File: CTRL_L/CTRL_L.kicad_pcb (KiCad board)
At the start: 2 copper layers, 33.8 x 93.2 mm, 22 parts, among them J1 BM14B-NSHSS-TBT_LF__SN_, J2 BM04B-NSHSS-TBT_LF__SN_, J3 BM04B-NSHSS-TBT_LF__SN_, SW3 SW_Push, SW4 SW_Push, SW5 SW_Push, SW6 SW_Push, SW7 SW_Push

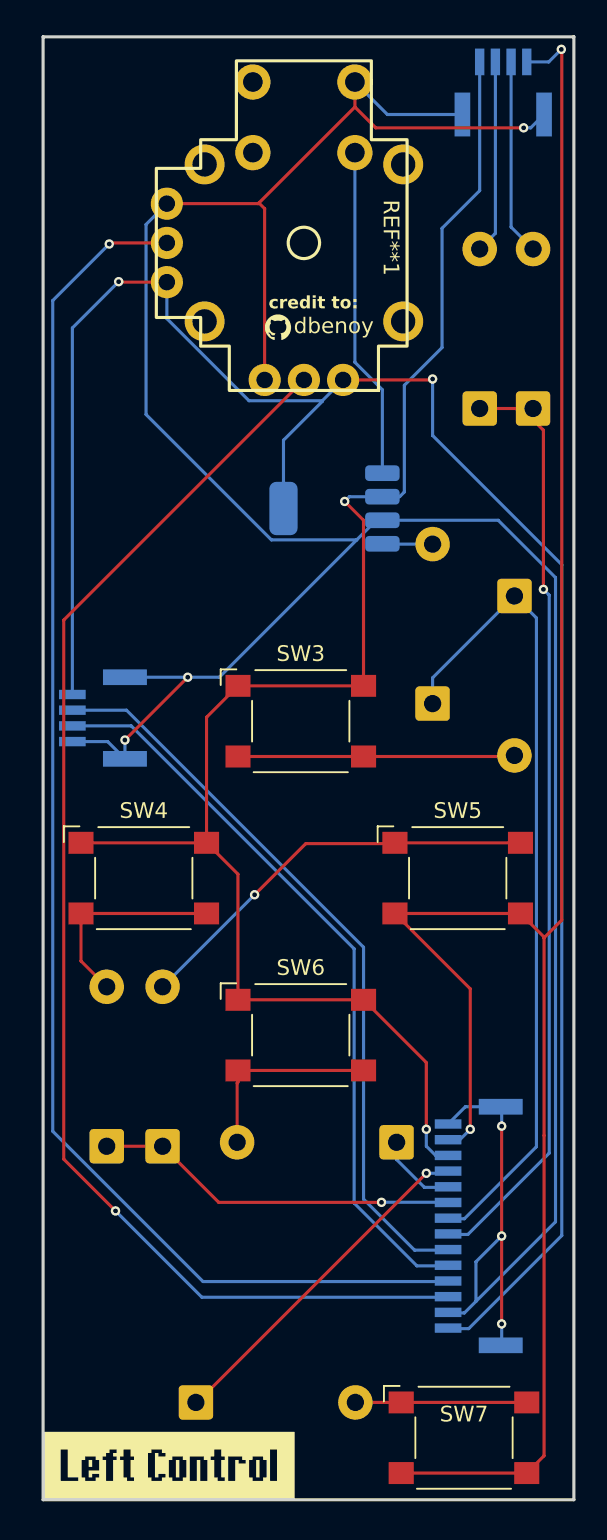
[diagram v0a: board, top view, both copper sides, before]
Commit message: CTRL_L updated to use new Diodes.
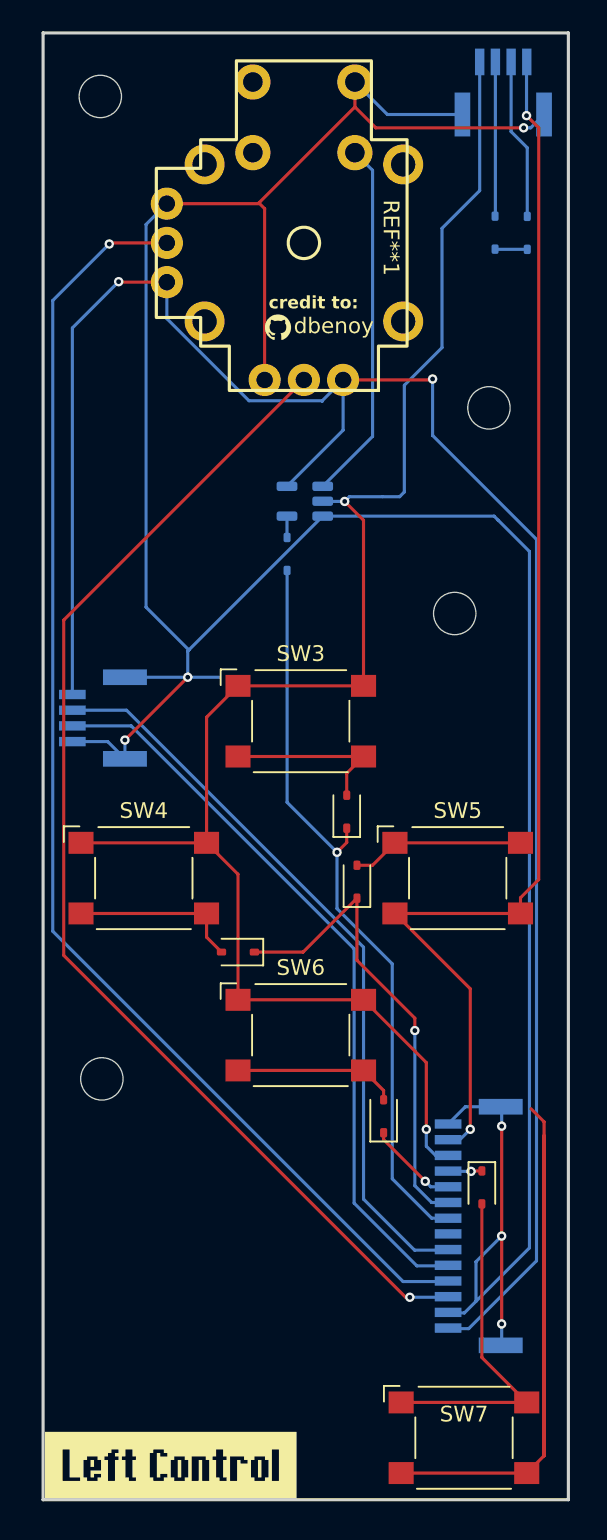
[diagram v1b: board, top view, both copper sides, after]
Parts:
- removed AND1: 74AHC1G08, Package_TO_SOT_SMD:SOT-223-5
- added REF**: M2.5_2.7mm, MountingHole:MountingHole_2.7mm_M2.5, F.Cu at (158.2, 72.1)
- added REF**: M2.5_2.7mm, MountingHole:MountingHole_2.7mm_M2.5, F.Cu at (135.6, 39.2)
- added REF**: M2.5_2.7mm, MountingHole:MountingHole_2.7mm_M2.5, F.Cu at (135.7, 101.8)
- added REF**: M2.5_2.7mm, MountingHole:MountingHole_2.7mm_M2.5, F.Cu at (160.4, 59.0)
- added U1: 74LVC1G08, Package_TO_SOT_SMD:SOT-23-5, B.Cu at (148.7, 65.0)
- D1, D2, D8: value 1N4001 -> 1N4148WS; footprint Diode_THT:D_DO-41_SOD81_P10.16mm_Horizontal -> Diode_SMD:D_SOD-323
- D3, D4, D5, D6, D7: value 1N4001 -> 1N4148WS; footprint Diode_THT:D_DO-41_SOD81_P10.16mm_Horizontal -> Diode_SMD:D_SOD-323; moved to F.Cu
- moved D8 54.4 mm to (147.5, 68.3), turned to 90 degrees
- moved D4 28.7 mm to (144.4, 93.7), turned to 180 degrees
- moved D5 23.2 mm to (152.0, 89.2)
- moved D6 14.2 mm to (153.7, 104.2)
- moved D1 11.2 mm to (160.8, 47.9)
- moved D2 11.2 mm to (162.8, 47.9)
- moved D3 8.80 mm to (151.3, 84.8)
- moved D7 6.15 mm to (159.9, 108.7), turned to -90 degrees
- moved kibuzzard-6A187131 0.46 mm to (157.3, 126.4)
- moved kibuzzard-6A186FEC 0.12 mm to (140.1, 126.4)
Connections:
- D4 pad 1: Row2 -> Row3
- D6 pad 1: Row3 -> Row4
- D7 pad 1: Row4 -> Row5
- D8 pad 1: Row5 -> Row2
- SW3 pad 2: Net-(D4-A) -> Net-(D3-A)
- SW4 pad 2: Net-(D5-A) -> Net-(D4-A)
- SW5 pad 1: Net-(D6-A) -> Net-(D5-A)
- SW6 pad 2: Net-(D7-A) -> Net-(D6-A)
- SW7 pad 1: Net-(D8-A) -> Net-(D7-A)
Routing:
- net Row1: track 59.9 -> 2.06 mm, vias 1 -> 0
- net Row5: track 22.1 -> 2.17 mm
- net Net-(D6-A): track 26.6 -> 10.4 mm, vias 1 -> 0
- net Net-(D8-A): track 10.9 -> 1.36 mm
- net Net-(D7-A): track 12.8 -> 21.8 mm
- net /ADC_X: track 84.1 -> 76.5 mm
- net /ADC_Y: track 90.9 -> 83.4 mm
- net Row3: track 23.3 -> 30.4 mm
- net Net-(D3-A): track 4.01 -> 10.9 mm
- net Net-(D4-A): track 17.7 -> 10.9 mm
- net Row2: track 52.2 -> 48.0 mm, vias 0 -> 1
- net Col2: track 130.0 -> 132.6 mm
- net Net-(D1-A): track 12.3 -> 9.84 mm
- net Net-(D5-A): track 13.5 -> 11.0 mm
- net Net-(D2-A): track 12.5 -> 10.3 mm
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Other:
- board size 33.8 x 93.2 mm -> 33.5 x 93.4 mm

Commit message: Added New Images (\Images)
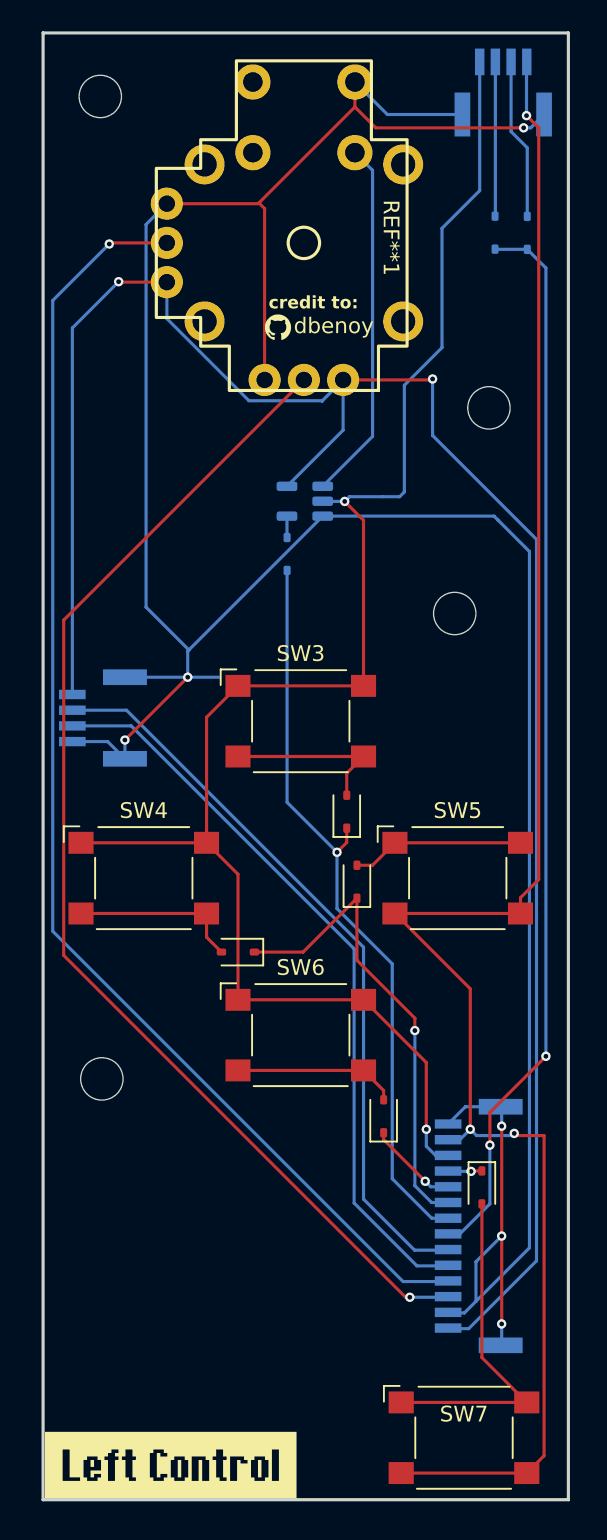
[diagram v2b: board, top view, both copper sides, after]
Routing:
- net Row1: track 2.06 -> 68.3 mm, vias 0 -> 2
- net Col2: track 132.6 -> 115.1 mm, vias 2 -> 3
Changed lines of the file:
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@@
-	)
-	(segment
-		(start 163.07 103.69)
-		(end 163.9 104.52)
-		(width 0.2)
-		(layer "F.Cu")
-		(net "Col2")
 	)
 	(segment
@@
 	)
 	(segment
+		(start 162.14 105.4)
+		(end 162 105.26)
+		(width 0.2)
+		(layer "F.Cu")
+		(net "Col2")
+	)
+	(segment
 		(start 162.4 91.25)
 		(end 162.4 91.64)
@@
 	)
 	(segment
+		(start 163.9 105.4)
+		(end 162.14 105.4)
+		(width 0.2)
+		(layer "F.Cu")
+		(net "Col2")
+	)
+	(segment
 		(start 162.783835 40.421406)
 		(end 163.56 41.197571)
@@
 		(net "Col2")
 	)
-	(segment
-		(start 163.9 104.52)
-		(end 163.9 125.8)
-		(width 0.2)
-		(layer "F.Cu")
-		(net "Col2")
-	)
 	(via
 		(at 159.2 105)
@@
 	)
 	(via
+		(at 162 105.26)
+		(size 0.6)
+		(drill 0.3)
+		(layers "F.Cu" "B.Cu")
+		(net "Col2")
+	)
+	(via
 		(at 162.783835 40.421406)
 		(size 0.6)
 		(drill 0.3)
 		(layers "F.Cu" "B.Cu")
+		(net "Col2")
+	)
+	(segment
+		(start 159.6 105.4)
+		(end 159.2 105)
+		(width 0.2)
+		(layer "B.Cu")
 		(net "Col2")
 	)
@@
 	)
 	(segment
+		(start 162 105.26)
+		(end 161.86 105.4)
+		(width 0.2)
+		(layer "B.Cu")
+		(net "Col2")
+	)
+	(segment
 		(start 162.783835 37.366163)
 		(end 162.8 37.349998)
@@
 	)
 	(segment
+		(start 161.86 105.4)
+		(end 159.6 105.4)
+		(width 0.2)
+		(layer "B.Cu")
+		(net "Col2")
+	)
+	(segment
+		(start 164.02 100.35)
+		(end 160.45 103.92)
+		(width 0.2)
+		(layer "F.Cu")
+		(net "Row1")
+	)
+	(segment
+		(start 160.45 103.92)
+		(end 160.45 106.01)
+		(width 0.2)
+		(layer "F.Cu")
+		(net "Row1")
+	)
+	(via
+		(at 164.02 100.35)
+		(size 0.6)
+		(drill 0.3)
+		(layers "F.Cu" "B.Cu")
+		(net "Row1")
+	)
+	(via
+		(at 160.45 106.01)
+		(size 0.6)
+		(drill 0.3)
+		(layers "F.Cu" "B.Cu")
+		(net "Row1")
+	)
+	(segment
+		(start 162.83 48.94)
+		(end 164.02 50.13)
+		(width 0.2)
+		(layer "B.Cu")
+		(net "Row1")
+	)
+	(segment
+		(start 164.02 50.13)
+		(end 164.02 100.35)
+		(width 0.2)
+		(layer "B.Cu")
+		(net "Row1")
+	)
+	(segment
+		(start 160.45 106.01)
+		(end 160.45 109.751823)
+		(width 0.2)
+		(layer "B.Cu")
+		(net "Row1")
+	)
+	(segment
+		(start 158.538901 111.662922)
+		(end 157.788901 111.662922)
+		(width 0.2)
+		(layer "B.Cu")
+		(net "Row1")
+	)
+	(segment
+		(start 160.45 109.751823)
+		(end 158.538901 111.662922)
+		(width 0.2)
+		(layer "B.Cu")
+		(net "Row1")
+	)
+	(segment

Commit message: Updated CTRL_L to use B3S-1000 Switches
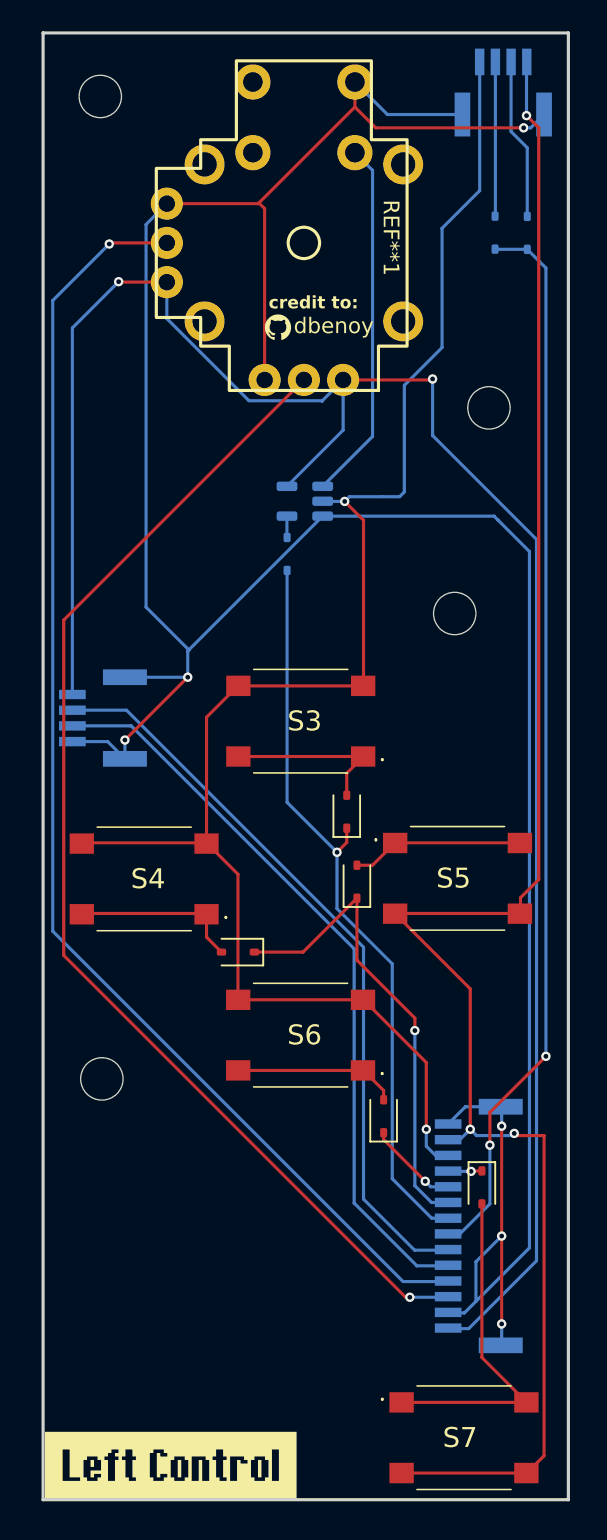
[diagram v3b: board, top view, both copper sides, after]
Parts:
- removed SW3, SW4, SW5, SW6, SW7: SW_Push, Button_Switch_SMD:SW_SPST_Omron_B3FS-100xP
- added S3: B3S-1000, B3S-1000:B3S1000, F.Cu at (148.4, 79.0)
- added S4: B3S-1000, B3S-1000:B3S1000, F.Cu at (138.4, 89.0)
- added S5: B3S-1000, B3S-1000:B3S1000, F.Cu at (158.4, 89.0)
- added S6: B3S-1000, B3S-1000:B3S1000, F.Cu at (148.4, 99.0)
- added S7: B3S-1000, B3S-1000:B3S1000, F.Cu at (158.8, 124.7)
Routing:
- net GND: track 197.9 -> 195.9 mm

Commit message: Mainboard Progress, Updated CTRL-L for new Joystick Module
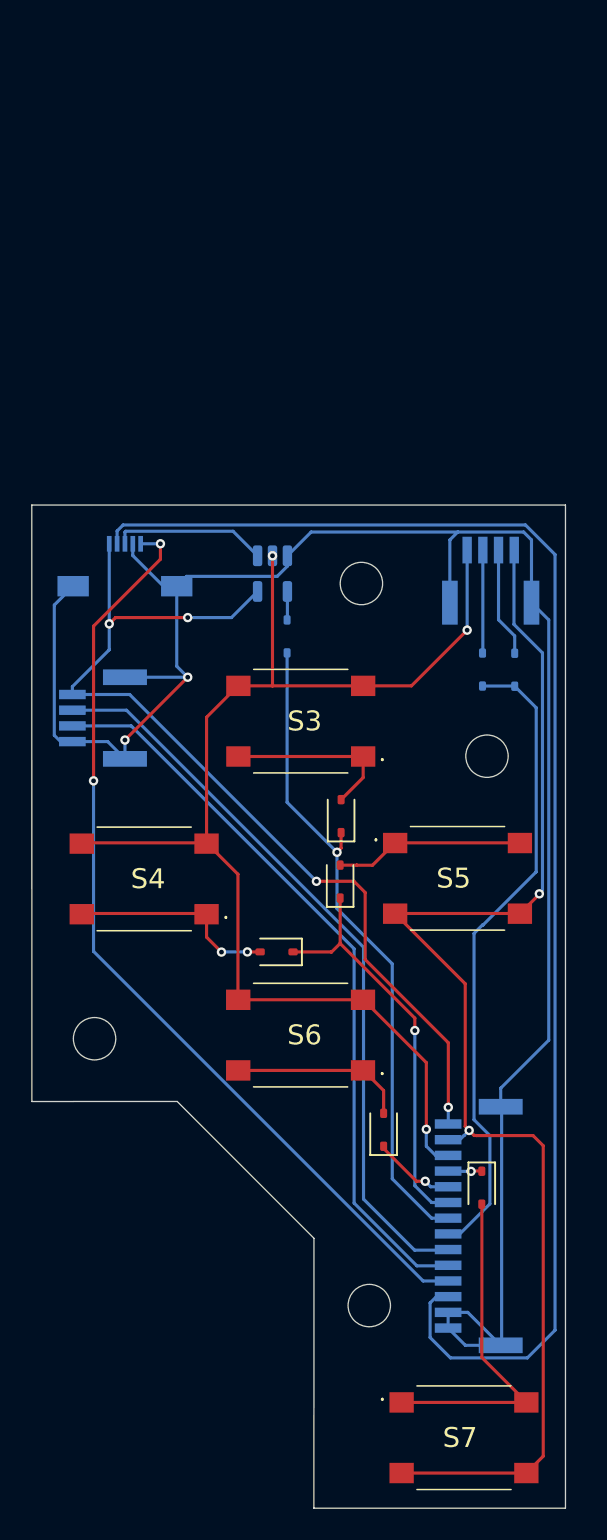
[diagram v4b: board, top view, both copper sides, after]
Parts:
- removed G***: LOGO, LOGO
- removed REF** (x4): M2.5_2.7mm, MountingHole:MountingHole_2.7mm_M2.5
- removed REF**: OSHW-Symbol_6.7x6mm_SilkScreen, Symbol:OSHW-Symbol_6.7x6mm_SilkScreen
- removed REF**1: PS5, Joystick:Joystick
- added H1: MountingHole, MountingHole:MountingHole_2.7mm_M2.5, F.Cu at (152.3, 70.2)
- added H2: MountingHole, MountingHole:MountingHole_2.7mm_M2.5, F.Cu at (160.3, 81.2)
- added H3: MountingHole, MountingHole:MountingHole_2.7mm_M2.5, F.Cu at (135.3, 99.2)
- added H4: MountingHole, MountingHole:MountingHole_2.7mm_M2.5, F.Cu at (152.8, 116.2)
- added J4: 5051100592, 5051100592:CON_5051100592_MOL, B.Cu at (137.2, 70.2)
- kibuzzard-6A186FEC: moved to B.Cu
- moved J2 31.1 mm to (160.5, 70.3)
- moved D1 27.8 mm to (160.0, 75.7)
- moved D2 27.8 mm to (162.0, 75.7)
- moved kibuzzard-6A186FEC 17.5 mm to (157.2, 122.7), turned to 180 degrees
- moved D8 5.25 mm to (147.5, 73.6)
- moved U1 5.05 mm to (146.6, 69.6), turned to -90 degrees
- moved D4 2.46 mm to (146.9, 93.7)
- moved D5 1.07 mm to (150.9, 89.2)
- moved D6 0.86 mm to (153.7, 105.0)
- moved kibuzzard-6A187131 0.64 mm to (157.3, 127.0)
- moved D3 0.46 mm to (151.0, 85.0)
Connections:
- J1 pad 1: +3V3 -> GND
- J1 pad 14: GND -> +3V3
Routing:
- net GND: track 195.9 -> 127.7 mm, vias 6 -> 2
- net +3V3: track 127.3 -> 61.7 mm, vias 2 -> 4
- net Col2: track 115.1 -> 83.2 mm, vias 3 -> 2
- net Row1: track 68.3 -> 40.4 mm, vias 2 -> 0
- net Col1: track 105.4 -> 79.8 mm, vias 2 -> 3
- net /ADC_Y: track 83.4 -> 60.3 mm, vias 1 -> 2
- net /ADC_X: track 76.5 -> 91.8 mm, vias 1 -> 0
- net /SW: track 23.0 -> 9.87 mm
- net Row2: track 48.0 -> 42.3 mm
- net Row3: track 30.4 -> 26.1 mm
- net Net-(D1-A): track 9.84 -> 6.57 mm
- net Net-(D2-A): track 10.3 -> 7.00 mm
- net Net-(D4-A): track 10.9 -> 13.3 mm, vias 0 -> 2
- net Net-(D5-A): track 11.0 -> 12.1 mm
- net Net-(D6-A): track 10.4 -> 11.3 mm
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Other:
- board size 33.5 x 93.4 mm -> 34 x 63.9 mm
- board text removed: "credit to:"
- board text removed: "dbenoy"

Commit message: Final Cleanup, CTRL-L Likely Complete!
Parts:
- moved kibuzzard-6A186FEC 0.05 mm to (157.3, 122.8)
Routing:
- net GND: track 127.7 -> 126.1 mm
- net /ADC_X: track 91.8 -> 91.1 mm
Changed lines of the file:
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@@
 			(at 0.25 0 0)
 			(layer "F.SilkS")
+			(hide yes)
 			(effects
 				(font
@@
 			(layer "F.Fab")
 		)
-		(fp_text user "${REFERENCE}"
-			(at 0.25 0 0)
-			(layer "F.Fab")
-			(effects
-				(font
-					(size 1.27 1.27)
-					(thickness 0.254)
-				)
-			)
-		)
 		(pad "1" smd rect
 			(at 3.975 2.25 270)
@@
 	(footprint "kibuzzard-6A186FEC"
 		(layer "B.Cu")
-		(at 157.241 122.719 180)
+		(at 157.254 122.769 180)
 		(descr "Generated with KiBuzzard")
 		(tags "kb_params=eyJBbGlnbm1lbnRDaG9pY2UiOiAiQ2VudGVyIiwgIkNhcExlZnRDaG9pY2UiOiAiWyIsICJDYXBSaWdodENob2ljZSI6ICJdIiwgIkZvbnRDb21ib0JveCI6ICJJdGhhY2EiLCAiSGVpZ2h0Q3RybCI6IDIuMCwgIkxheWVyQ29tYm9Cb3giOiAiRi5TaWxrUyIsICJMaW5lU3BhY2luZ0N0cmwiOiAxLjUsICJNdWx0aUxpbmVUZXh0IjogIkxlZnQgQ29udHJvbCIsICJQYWRkaW5nQm90dG9tQ3RybCI6IDMuOCwgIlBhZGRpbmdMZWZ0Q3RybCI6IDMuOCwgIlBhZGRpbmdSaWdodEN0cmwiOiAzLjgsICJQYWRkaW5nVG9wQ3RybCI6IDMuOCwgIldpZHRoQ3RybCI6IDAuMCwgImFkdmFuY2VkQ2hlY2tib3giOiB0cnVlLCAiaW5saW5lRm9ybWF0VGV4dGJveCI6IGZhbHNlLCAibGluZW92ZXJTdHlsZUNob2ljZSI6ICJSb3VuZGVkIiwgImxpbmVvdmVyVGhpY2tuZXNzQ3RybCI6IDF9")
@@
 		(layer "Edge.Cuts")
 	)
-	(dimension
-		(type orthogonal)
-		(layer "Dwgs.User")
-		(pts
-			(xy 167.4574 48.6) (xy 169.0574 78.6)
-		)
-		(height 0.0574)
-		(orientation 1)
-		(format
-			(prefix "")
-			(suffix "")
-			(units 3)
-			(units_format 0)
-			(precision 4)
-			(suppress_zeroes yes)
-		)
-		(style
-			(thickness 0.2)
-			(arrow_length 1.27)
-			(text_position_mode 2)
-			(arrow_direction outward)
-			(extension_height 0.58642)
-			(extension_offset 0.5)
-			(keep_text_aligned yes)
-		)
-		(gr_text "30"
-			(at 167.6 63.6 90)
-			(layer "Dwgs.User")
-			(effects
-				(font
-					(size 1.5 1.5)
-					(thickness 0.3)
-				)
-			)
-		)
-	)
-	(dimension
-		(type orthogonal)
-		(layer "Dwgs.User")
-		(pts
-			(xy 167.6 78.6) (xy 169.0574 98.6)
-		)
-		(height -0.049533)
-		(orientation 1)
-		(format
-			(prefix "")
-			(suffix "")
-			(units 3)
-			(units_format 0)
-			(precision 4)
-			(suppress_zeroes yes)
-		)
-		(style
-			(thickness 0.2)
-			(arrow_length 1.27)
-			(text_position_mode 2)
-			(arrow_direction outward)
-			(extension_height 0.58642)
-			(extension_offset 0.5)
-			(keep_text_aligned yes)
-		)
-		(gr_text "20"
-			(at 167.6 88.6 90)
-			(layer "Dwgs.User")
-			(effects
-				(font
-					(size 1.5 1.5)
-					(thickness 0.3)
-				)
-			)
-		)
-	)
 	(point
 		(at 160.237 81.2)
@@
 	)
 	(segment
-		(start 160.486 81.374)
-		(end 160.499 81.374)
-		(width 0.2)
-		(layer "F.Cu")
-		(net "")
-	)
-	(segment
-		(start 150.97 84)
-		(end 150.99 84)
-		(width 0.2)
-		(layer "F.Cu")
-		(net "Net-(D3-A)")
-	)
-	(segment
 		(start 152.375 82.595)
 		(end 150.97 84)
@@
 	)
 	(segment
-		(start 153.68 106.08)
-		(end 153.68 106.22)
-		(width 0.2)
-		(layer "F.Cu")
-		(net "Row4")
-	)
-	(segment
 		(start 155.77 108.31)
 		(end 156.33 108.31)
@@
 	)
 	(segment
+		(start 154.412721 91.262721)
+		(end 159.126862 95.976862)
+		(width 0.2)
+		(layer "F.Cu")
+		(net "Col2")
+	)
+	(segment
 		(start 163.85 125.825)
 		(end 162.775 126.9)
@@
 	(segment
 		(start 159.126862 105.071992)
-		(end 158.878 104.82313)
-		(width 0.2)
-		(layer "F.Cu")
-		(net "Col2")
-	)
-	(segment
-		(start 158.878 104.82313)
-		(end 158.878 95.728)
-		(width 0.2)
-		(layer "F.Cu")
-		(net "Col2")
-	)
-	(segment
-		(start 159.126862 105.071992)
 		(end 159.449511 105.394641)
 		(width 0.2)
@@
 	)
 	(segment
-		(start 158.878 95.728)
-		(end 154.4 91.25)
+		(start 159.126862 95.976862)
+		(end 159.126862 105.071992)
 		(width 0.2)
 		(layer "F.Cu")
@@
 	)
 	(segment
-		(start 151.03 86.1)
-		(end 150.97 86.1)
-		(width 0.2)
-		(layer "F.Cu")
-		(net "Row2")
-	)
-	(segment
 		(start 150.97 87.09)
 		(end 150.71 87.35)
@@
 	)
 	(segment
-		(start 162.0175 76.76)
-		(end 162.03 76.7725)
-		(width 0.2)
-		(layer "B.Cu")
-		(net "Row1")
-	)
-	(segment
 		(start 160.45 109.751823)
 		(end 158.538901 111.662922)
@@
 	)
 	(segment
-		(start 160 74.64)
-		(end 159.98 74.66)
-		(width 0.2)
-		(layer "B.Cu")
-		(net "Net-(D1-A)")
-	)
-	(segment
 		(start 137.2 80.2)
 		(end 141.2 76.2)
@@
 	)
 	(segment
-		(start 133.1 80.3)
-		(end 133.85 80.3)
-		(width 0.2)
-		(layer "B.Cu")
-		(net "GND")
-	)
-	(segment
 		(start 141.124998 69.775)
 		(end 140.499998 70.4)
@@
 	)
 	(segment
-		(start 139.65 70.4)
-		(end 140.499998 70.4)
-		(width 0.2)
-		(layer "B.Cu")
-		(net "GND")
-	)
-	(segment
 		(start 164.2 72.55)
 		(end 164.2 99.321471)
@@
 	)
 	(segment
-		(start 147.55 72.53)
-		(end 147.53 72.55)
-		(width 0.2)
-		(layer "B.Cu")
-		(net "Net-(D8-A)")
-	)
-	(segment
 		(start 149.4 89.2)
 		(end 151.78898 89.2)
@@
 	)
 	(segment
-		(start 133.85 77.3)
-		(end 137.5 77.3)
+		(start 148.784 89.2)
+		(end 149.4 89.2)
+		(width 0.2)
+		(layer "B.Cu")
+		(net "+3V3")
+	)
+	(segment
+		(start 136.884 77.3)
+		(end 148.784 89.2)
 		(width 0.2)
 		(layer "B.Cu")
@@
 	)
 	(segment
+		(start 133.85 77.3)
+		(end 136.884 77.3)
+		(width 0.2)
+		(layer "B.Cu")
+		(net "+3V3")
+	)
+	(segment
 		(start 145.65 70.7375)
 		(end 143.9875 72.4)
@@
 	)
 	(segment
-		(start 137.5 77.3)
-		(end 149.4 89.2)
-		(width 0.2)
-		(layer "B.Cu")
-		(net "+3V3")
-	)
-	(segment
-		(start 157.8 104.651823)
-		(end 157.788901 104.662922)
-		(width 0.2)
-		(layer "B.Cu")
-		(net "+3V3")
-	)
-	(segment
 		(start 151.8 93.5)
 		(end 151.8 109.7)
@@
 	)
 	(segment
-		(start 157.038901 115.662922)
-		(end 157.788901 115.662922)
-		(width 0.2)
-		(layer "B.Cu")
-		(net "/ADC_X")
-	)
-	(segment
 		(start 162.838901 119.562922)
 		(end 157.938901 119.562922)
@@
 		(width 0.2)
 		(layer "B.Cu")
-		(net "/ADC_Y")
-	)
-	(segment
-		(start 138.20177 67.698232)
-		(end 138.200001 67.700001)
-		(width 0.2)
-		(layer "B.Cu")
